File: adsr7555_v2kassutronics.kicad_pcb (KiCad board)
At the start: 2 copper layers, 78.7 x 106.7 mm, 43 parts, among them J1 Power, J2 GateIn, J5 InvOut, J6 Output, Q1 3904, Q2 3904, Q3 3904, SW1 SW_Trig, U1 7555, U2 TL074

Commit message: wiring TL074 needs checking
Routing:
- net GND: track 336.9 -> 340.5 mm, vias 2 -> 4
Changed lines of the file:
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@@
 		(tags "Resistor Axial_DIN0204 series Axial Horizontal pin pitch 7.62mm 0.167W length 3.6mm diameter 1.6mm")
 		(property "Reference" "R16"
-			(at 10.5 0.24 90)
+			(at 0 2.54 180)
 			(layer "F.SilkS")
 			(effects
@@
 		)
 		(property "Value" "1k"
-			(at 9.2 0.44 90)
+			(at 5.08 2.54 180)
 			(layer "F.Fab")
 			(effects
@@
 	)
 	(segment
+		(start 106.68 86.36)
+		(end 104.14 88.9)
+		(width 0.5)
+		(layer "F.Cu")
+		(net "GND")
+	)
+	(segment
 		(start 109.22 83.82)
 		(end 114.3 83.82)
@@
 		(net "GND")
 	)
+	(segment
+		(start 104.14 88.9)
+		(end 86.36 88.9)
+		(width 0.5)
+		(layer "F.Cu")
+		(net "GND")
+	)
+	(via
+		(at 86.36 88.9)
+		(size 0.6)
+		(drill 0.3)
+		(layers "F.Cu" "B.Cu")
+		(net "GND")
+	)
 	(via
 		(at 109.22 83.82)
@@
 	)
 	(via
-		(at 114.3 127)
+		(at 106.68 86.36)
 		(size 0.6)
 		(drill 0.3)
@@
 		(net "GND")
 	)
-	(segment
-		(start 109.22 83.82)
-		(end 101.6 83.82)
-		(width 0.5)
-		(layer "B.Cu")
+	(via
+		(at 114.3 127)
+		(size 0.6)
+		(drill 0.3)
+		(layers "F.Cu" "B.Cu")
 		(net "GND")
 	)
@@
 	)
 	(segment
+		(start 109.22 83.82)
+		(end 106.68 86.36)
+		(width 0.5)
+		(layer "B.Cu")
+		(net "GND")
+	)
+	(segment
 		(start 109.22 30.48)
 		(end 109.22 33.02)
@@
 	)
 	(segment
+		(start 86.36 83.82)
+		(end 86.36 88.9)
+		(width 0.5)
+		(layer "B.Cu")
+		(net "GND")
+	)
+	(segment
 		(start 96.52 114.3)
 		(end 93.98 116.84)
@@
 	)
 	(segment
-		(start 86.36 81.28)
-		(end 86.36 83.82)
-		(width 0.5)
-		(layer "B.Cu")
-		(net "GND")
-	)
-	(segment
 		(start 48.3 101.6)
 		(end 45.72 101.6)
@@
 	)
 	(segment
-		(start 101.6 83.82)
-		(end 99.06 81.28)
-		(width 0.5)
-		(layer "B.Cu")
-		(net "GND")
-	)
-	(segment
 		(start 48.26 66.04)
 		(end 45.72 66.04)
@@
 	)
 	(segment
-		(start 99.06 81.28)
-		(end 86.36 81.28)
-		(width 0.5)
-		(layer "B.Cu")
-		(net "GND")
-	)
-	(segment
 		(start 45.72 43.18)
 		(end 60.96 30.48)
@@
 	(segment
 		(start 76.2 88.9)
-		(end 76.2 109.22)
+		(end 76.2 101.6)
 		(width 0.5)
 		(layer "F.Cu")
@@
 	)
 	(via
-		(at 76.2 109.22)
+		(at 76.2 101.6)
 		(size 0.6)
 		(drill 0.3)
@@
 	)
 	(segment
-		(start 91.44 78.74)
-		(end 76.2 78.74)
+		(start 76.2 101.6)
+		(end 76.2 109.22)
 		(width 0.5)
 		(layer "B.Cu")
@@
 	)
 	(segment
-		(start 88.9 111.76)
-		(end 88.9 124.46)
+		(start 91.44 78.74)
+		(end 76.2 78.74)
 		(width 0.5)
 		(layer "B.Cu")
@@
 	)
 	(segment
-		(start 76.2 109.22)
-		(end 81.28 109.22)
+		(start 88.9 111.76)
+		(end 88.9 124.46)
 		(width 0.5)
 		(layer "B.Cu")
@@
 	)
 	(segment
-		(start 81.28 109.22)
-		(end 83.82 111.76)
+		(start 91.44 76.2)
+		(end 91.44 78.74)
 		(width 0.5)
 		(layer "B.Cu")
@@
 	)
 	(segment
-		(start 91.44 76.2)
-		(end 91.44 78.74)
+		(start 76.2 109.22)
+		(end 81.28 109.22)
+		(width 0.5)
+		(layer "B.Cu")
+		(net "THR")
+	)
+	(segment
+		(start 83.82 111.76)
+		(end 81.28 109.22)
 		(width 0.5)
 		(layer "B.Cu")

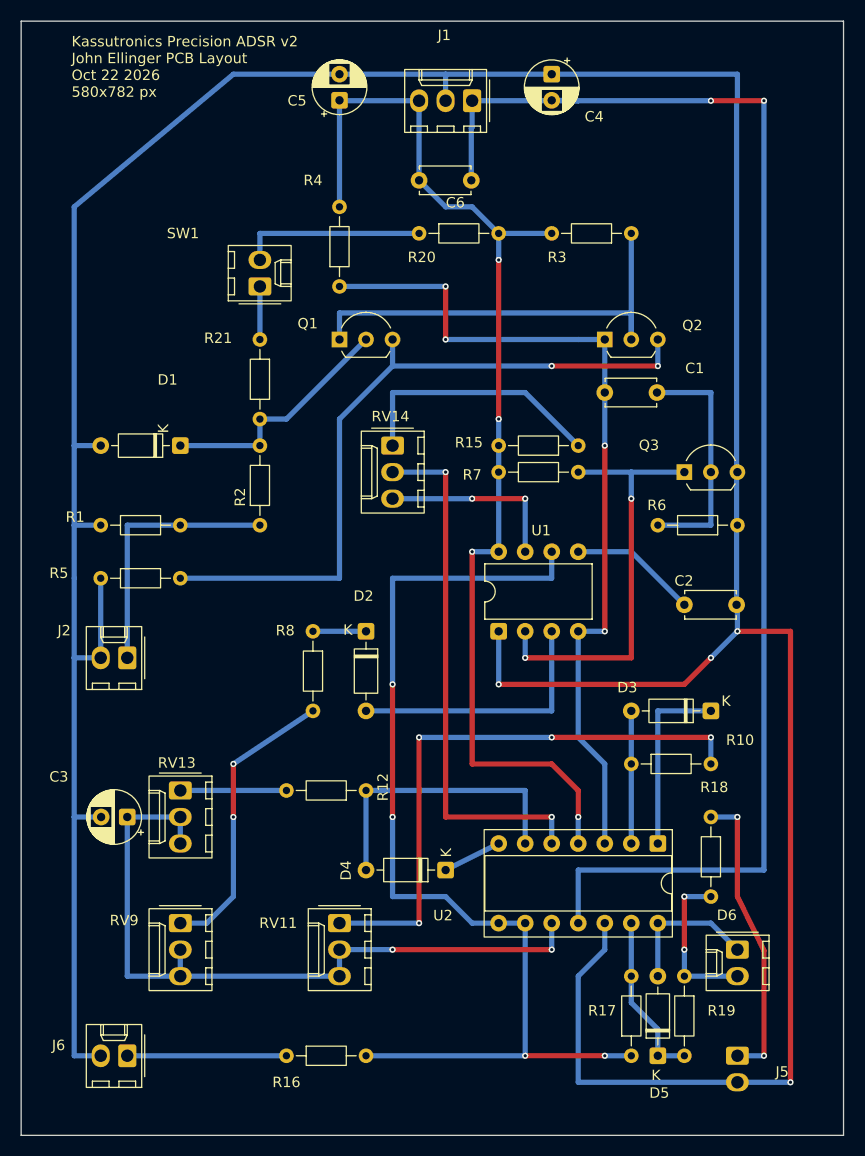
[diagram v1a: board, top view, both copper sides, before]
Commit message: MAJOR FUP U2 was positioned backwards. Involved pt to pt silicon wires on bottom of PCB. Still not done
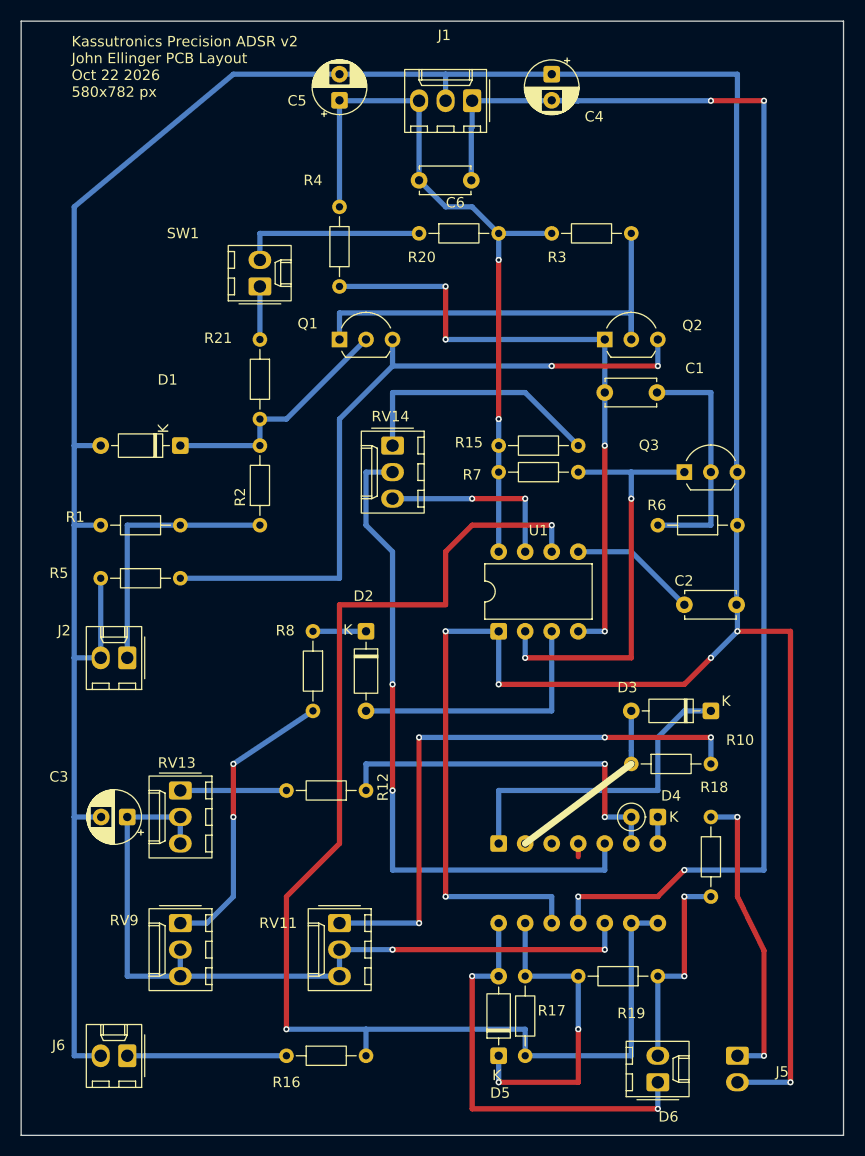
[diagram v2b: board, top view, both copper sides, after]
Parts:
- D4: footprint Diode_THT:D_DO-35_SOD27_P7.62mm_Horizontal -> Diode_THT:D_DO-35_SOD27_P2.54mm_Vertical_CathodeUp
- U2: moved to B.Cu
- moved D4 20.9 mm to (101.6, 101.6)
- moved D5 15.2 mm to (86.4, 124.5)
- moved U2 15.2 mm to (86.4, 104.1)
- moved D6 14.8 mm to (101.6, 127.0), turned to 90 degrees
- moved R17 10.2 mm to (88.9, 124.5)
- moved R19 2.54 mm to (101.6, 116.8), turned to 180 degrees
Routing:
- net +15V: track 109.9 -> 72.0 mm, vias 4 -> 2
- net Net-(D5-A): track 13.8 -> 40.6 mm, vias 0 -> 2
- net THR: track 100.1 -> 125.1 mm, vias 4 -> 2
- net GATE: track 82.3 -> 61.0 mm
- net Net-(D5-K): track 16.3 -> 30.5 mm, vias 0 -> 2
- net Net-(U2B-+): track 50.8 -> 64.6 mm
- net Net-(D3-K): track 17.8 -> 31.5 mm
- net GND: track 340.5 -> 352.1 mm, vias 4 -> 6
- net Net-(D4-A): track 27.9 -> 35.6 mm, vias 0 -> 2
- net Net-(D3-A): track 12.7 -> 5.08 mm
- net Net-(D6-A): track 15.2 -> 20.3 mm
- net Net-(U2C-+): track 71.1 -> 76.2 mm
- net Net-(D4-K): track 5.68 -> 2.54 mm
- net -15V: track 134.7 -> 133.2 mm, vias 2 -> 4
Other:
- board text added: "1"

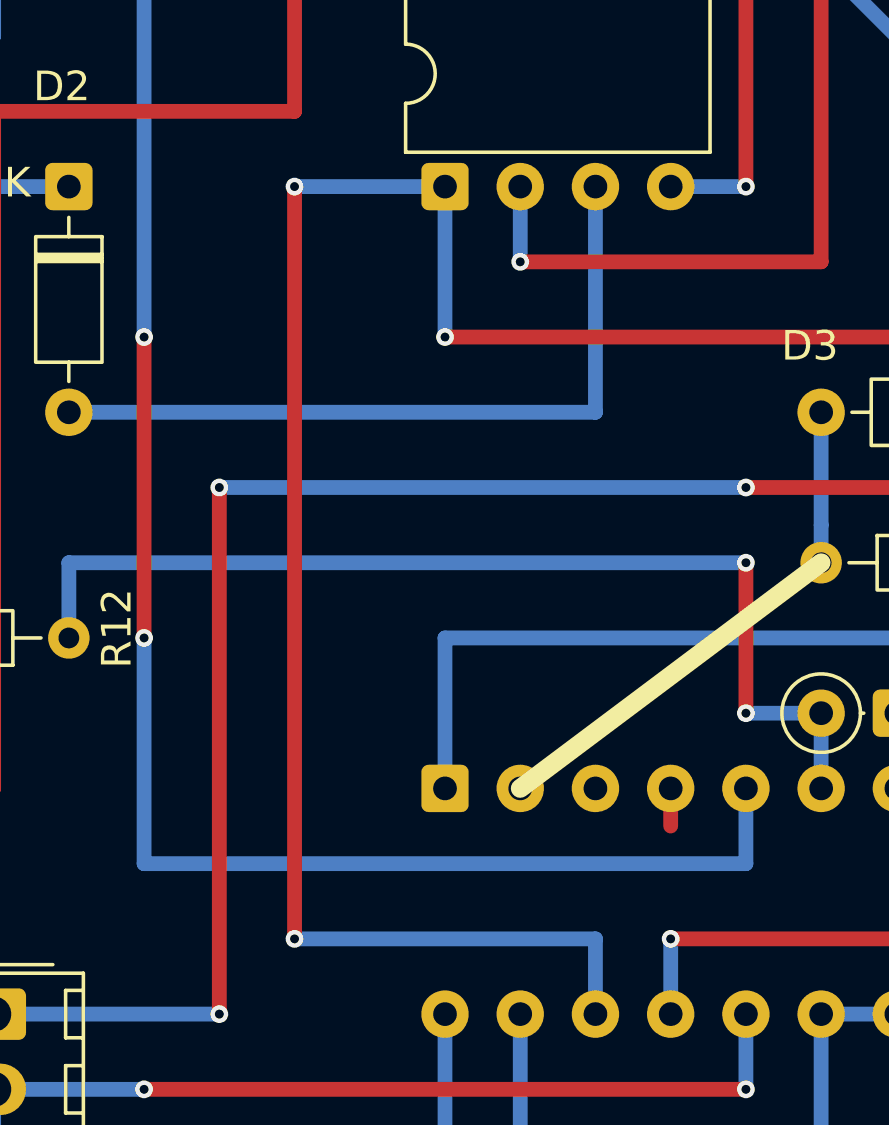
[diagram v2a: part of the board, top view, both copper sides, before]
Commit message: wired +15 -15 gnd
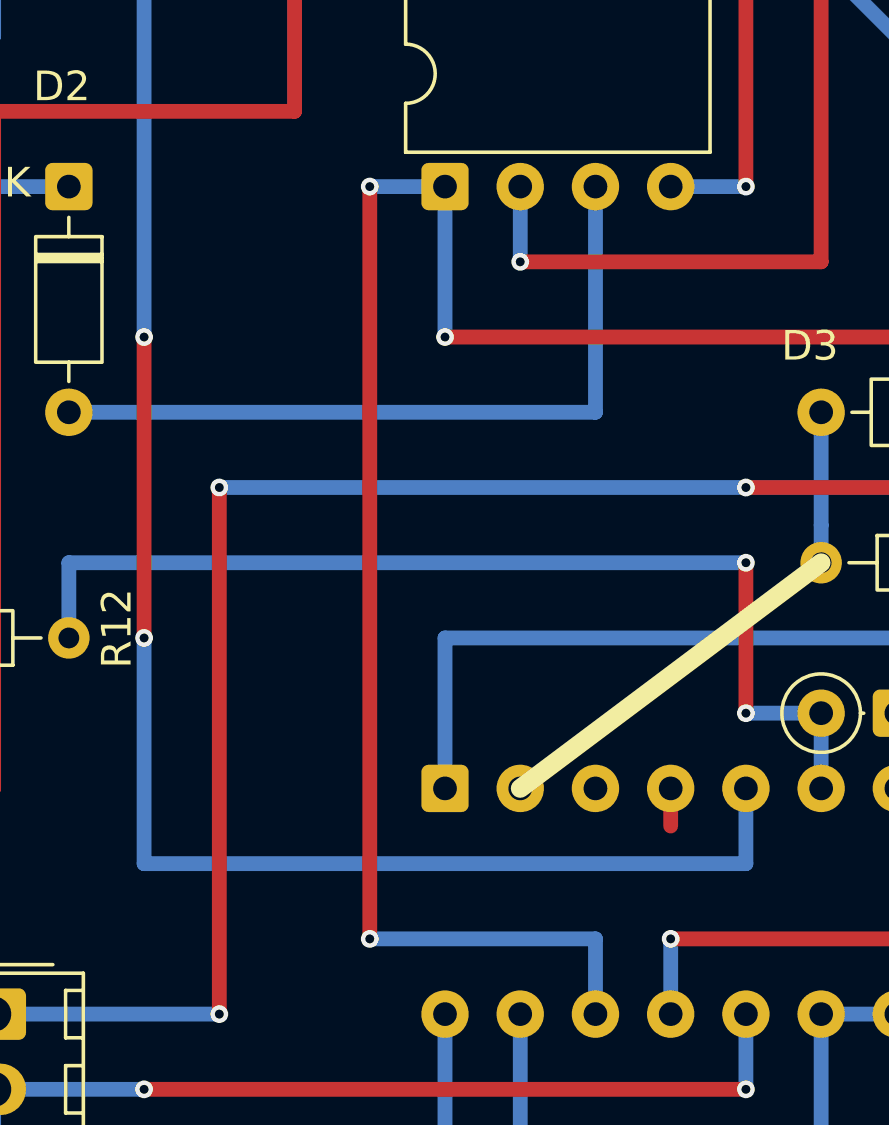
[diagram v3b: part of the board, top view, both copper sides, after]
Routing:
- net GND: track 352.1 -> 347.1 mm

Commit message: wiring L074 area in progress
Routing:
- net THR: track 125.1 -> 111.8 mm, vias 2 -> 4
- net Net-(D3-K): track 31.5 -> 40.6 mm
- net Net-(U2B-+): track 64.6 -> 61.0 mm, vias 2 -> 4
- net Net-(J5-Pin_1): track 28.5 -> 27.9 mm
- net -15V: vias 4 -> 2
- net Net-(D6-A): vias 2 -> 0
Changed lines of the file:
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@@
 			(at -1.62 0.32 90)
 			(layer "F.SilkS")
+			(hide yes)
 			(effects
 				(font
@@
 	)
 	(segment
-		(start 71.12 104.14)
-		(end 71.12 81.28)
-		(width 0.5)
-		(layer "F.Cu")
-		(net "THR")
-	)
-	(segment
-		(start 66.04 121.92)
-		(end 66.04 109.22)
+		(start 76.2 73.66)
+		(end 76.2 119.38)
 		(width 0.5)
 		(layer "F.Cu")
@@
 	)
 	(segment
-		(start 81.28 76.2)
-		(end 83.82 73.66)
-		(width 0.5)
-		(layer "F.Cu")
-		(net "THR")
-	)
-	(segment
-		(start 66.04 109.22)
-		(end 71.12 104.14)
-		(width 0.5)
-		(layer "F.Cu")
-		(net "THR")
-	)
-	(segment
-		(start 71.12 81.28)
-		(end 81.28 81.28)
+		(start 83.82 73.66)
+		(end 91.44 73.66)
 		(width 0.5)
 		(layer "F.Cu")
 		(net "THR")
 	)
-	(segment
-		(start 81.28 81.28)
-		(end 81.28 76.2)
-		(width 0.5)
-		(layer "F.Cu")
+	(via
+		(at 83.82 73.66)
+		(size 0.6)
+		(drill 0.3)
+		(layers "F.Cu" "B.Cu")
 		(net "THR")
 	)
-	(segment
-		(start 83.82 73.66)
-		(end 91.44 73.66)
-		(width 0.5)
-		(layer "F.Cu")
+	(via
+		(at 76.2 119.38)
+		(size 0.6)
+		(drill 0.3)
+		(layers "F.Cu" "B.Cu")
 		(net "THR")
 	)
 	(via
-		(at 66.04 121.92)
+		(at 76.2 73.66)
 		(size 0.6)
 		(drill 0.3)
@@
 	)
 	(segment
-		(start 73.66 121.92)
-		(end 88.9 121.92)
+		(start 76.2 121.92)
+		(end 78.74 121.92)
 		(width 0.5)
 		(layer "B.Cu")
@@
 	)
 	(segment
-		(start 73.66 121.92)
-		(end 66.04 121.92)
+		(start 91.44 76.2)
+		(end 91.44 73.66)
 		(width 0.5)
 		(layer "B.Cu")
@@
 	)
 	(segment
-		(start 91.44 76.2)
-		(end 91.44 73.66)
+		(start 78.74 121.92)
+		(end 88.9 121.92)
 		(width 0.5)
 		(layer "B.Cu")
@@
 	)
 	(segment
+		(start 76.2 121.92)
+		(end 76.2 119.38)
+		(width 0.5)
+		(layer "B.Cu")
+		(net "THR")
+	)
+	(segment
+		(start 83.82 73.66)
+		(end 76.2 73.66)
+		(width 0.5)
+		(layer "B.Cu")
+		(net "THR")
+	)
+	(segment
 		(start 73.66 124.46)
 		(end 73.66 121.92)
@@
 	)
 	(segment
+		(start 73.66 121.92)
+		(end 76.2 121.92)
+		(width 0.5)
+		(layer "B.Cu")
+		(net "THR")
+	)
+	(segment
 		(start 99.06 124.46)
 		(end 99.06 111.76)
@@
 	)
 	(segment
-		(start 76.2 114.3)
+		(start 78.74 114.3)
 		(end 96.52 114.3)
 		(width 0.5)
@@
 	)
 	(via
-		(at 76.2 114.3)
+		(at 78.74 114.3)
 		(size 0.6)
 		(drill 0.3)
@@
 	(segment
 		(start 71.12 114.3)
-		(end 76.2 114.3)
+		(end 78.74 114.3)
 		(width 0.5)
 		(layer "B.Cu")
@@
 		(net "Net-(J5-Pin_1)")
 	)
-	(segment
-		(start 111.76 114.378122)
-		(end 111.76 124.46)
-		(width 0.5)
-		(layer "F.Cu")
-		(net "Net-(J5-Pin_1)")
-	)
-	(segment
-		(start 109.22 109.22)
-		(end 111.76 114.378122)
-		(width 0.5)
-		(layer "F.Cu")
-		(net "Net-(J5-Pin_1)")
-	)
 	(via
 		(at 109.22 101.6)
@@
 	)
 	(via
-		(at 111.76 124.46)
+		(at 109.22 109.22)
 		(size 0.6)
 		(drill 0.3)
@@
 	)
 	(segment
+		(start 109.22 124.46)
+		(end 109.22 109.22)
+		(width 0.5)
+		(layer "B.Cu")
+		(net "Net-(J5-Pin_1)")
+	)
+	(segment
 		(start 111.76 124.46)
 		(end 109.22 124.46)
@@
 	)
 	(segment
-		(start 104.14 116.84)
-		(end 104.14 109.22)
+		(start 101.6 124.46)
+		(end 101.6 116.84)
 		(width 0.5)
-		(layer "F.Cu")
-		(net "Net-(D6-A)")
-	)
-	(via
-		(at 104.14 116.84)
-		(size 0.6)
-		(drill 0.3)
-		(layers "F.Cu" "B.Cu")
-		(net "Net-(D6-A)")
-	)
-	(via
-		(at 104.14 109.22)
-		(size 0.6)
-		(drill 0.3)
-		(layers "F.Cu" "B.Cu")
+		(layer "B.Cu")
 		(net "Net-(D6-A)")
 	)
 	(segment
-		(start 101.6 124.46)
-		(end 101.6 116.84)
+		(start 104.14 109.22)
+		(end 106.68 109.22)
 		(width 0.5)
 		(layer "B.Cu")
@@
 	(segment
 		(start 104.14 109.22)
-		(end 106.68 109.22)
+		(end 104.14 116.84)
 		(width 0.5)
 		(layer "B.Cu")
@@
 	)
 	(segment
-		(start 76.2 99.06)
-		(end 76.2 88.9)
+		(start 81.28 88.9)
+		(end 81.28 106.68)
+		(width 0.5)
+		(layer "F.Cu")
+		(net "Net-(U2B-+)")
+	)
+	(segment
+		(start 81.28 68.58)
+		(end 81.28 86.36)
 		(width 0.5)
 		(layer "F.Cu")
@@
 	)
 	(via
-		(at 76.2 99.06)
+		(at 81.28 68.58)
 		(size 0.6)
 		(drill 0.3)
@@
 	)
 	(via
-		(at 76.2 88.9)
+		(at 81.28 106.68)
 		(size 0.6)
 		(drill 0.3)
@@
 		(net "Net-(U2B-+)")
 	)
-	(segment
-		(start 96.52 104.14)
-		(end 96.52 106.68)
-		(width 0.5)
-		(layer "B.Cu")
-		(net "Net-(U2B-+)")
-	)
-	(segment
-		(start 96.52 106.68)
-		(end 76.2 106.68)
-		(width 0.5)
-		(layer "B.Cu")
+	(via
+		(at 81.28 86.36)
+		(size 0.6)
+		(drill 0.3)
+		(layers "F.Cu" "B.Cu")
 		(net "Net-(U2B-+)")
 	)
-	(segment
-		(start 76.2 88.9)
-		(end 76.2 76.2)
-		(width 0.5)
-		(layer "B.Cu")
+	(via
+		(at 81.28 88.9)
+		(size 0.6)
+		(drill 0.3)
+		(layers "F.Cu" "B.Cu")
 		(net "Net-(U2B-+)")
 	)
 	(segment
-		(start 76.2 76.2)
-		(end 73.66 73.66)
+		(start 76.2 68.58)
+		(end 81.28 68.58)
 		(width 0.5)
 		(layer "B.Cu")
@@
 	)
 	(segment
-		(start 73.66 68.58)
-		(end 76.2 68.58)
+		(start 96.52 106.68)
+		(end 96.52 104.14)
 		(width 0.5)
 		(layer "B.Cu")
@@
 	)
 	(segment
-		(start 73.66 73.66)
-		(end 73.66 68.58)
+		(start 81.28 86.36)
+		(end 81.28 88.9)
 		(width 0.5)
 		(layer "B.Cu")
@@
 	)
 	(segment
-		(start 76.2 106.68)
-		(end 76.2 99.06)
+		(start 81.28 106.68)
+		(end 96.52 106.68)
 		(width 0.5)
 		(layer "B.Cu")
@@
 	)
 	(segment
-		(start 101.6 93.98)
-		(end 104.14 91.44)
-		(width 0.5)
-		(layer "B.Cu")
-		(net "Net-(D3-K)")
-	)
-	(segment
 		(start 86.36 104.14)
 		(end 86.36 99.06)
@@
 	)
 	(segment
-		(start 101.6 99.06)
-		(end 101.6 93.98)
+		(start 104.14 91.44)
+		(end 106.68 91.44)
 		(width 0.5)
 		(layer "B.Cu")
@@
 	)
 	(segment
-		(start 104.14 91.44)
+		(start 109.22 91.44)
 		(end 106.68 91.44)
 		(width 0.5)
@@
 	)
 	(segment
-		(start 86.36 99.06)
-		(end 101.6 99.06)
+		(start 109.22 99.06)
+		(end 109.22 91.44)
 		(width 0.5)
 		(layer "B.Cu")
@@
 	)
 	(segment
-		(start 104.14 106.68)
-		(end 101.6 109.22)
-		(width 0.5)
-		(layer "F.Cu")
-		(net "-15V")
-	)
-	(segment
-		(start 101.6 109.22)
-		(end 93.98 109.22)
+		(start 86.36 99.06)
+		(end 109.22 99.06)
 		(width 0.5)
-		(layer "F.Cu")
-		(net "-15V")
+		(layer "B.Cu")
+		(net "Net-(D3-K)")
 	)
 	(segment
@@
 		(net "-15V")
 	)
-	(via
-		(at 93.98 109.22)
-		(size 0.6)
-		(drill 0.3)
-		(layers "F.Cu" "B.Cu")
-		(net "-15V")
-	)
-	(via
-		(at 104.14 106.68)
-		(size 0.6)
-		(drill 0.3)
-		(layers "F.Cu" "B.Cu")
-		(net "-15V")
-	)
 	(segment
-		(start 93.98 109.22)
-		(end 93.98 111.76)
+		(start 111.76 106.68)
+		(end 111.76 33.02)
 		(width 0.5)
 		(layer "B.Cu")
@@
 	)
 	(segment
-		(start 91.44 32.98)
-		(end 93.98 33.02)
+		(start 93.98 109.22)
+		(end 99.06 109.22)
 		(width 0.5)
 		(layer "B.Cu")
@@
 	)
 	(segment
-		(start 111.76 106.68)
-		(end 104.14 106.68)
+		(start 91.44 32.98)
+		(end 93.98 33.02)
 		(width 0.5)
 		(layer "B.Cu")
@@
 	)
 	(segment
-		(start 93.98 33.02)
-		(end 106.68 33.02)
+		(start 93.98 111.76)
+		(end 93.98 109.22)
 		(width 0.5)
 		(layer "B.Cu")
@@
 	)
 	(segment
-		(start 111.76 33.02)
-		(end 111.76 106.68)
+		(start 93.98 33.02)
+		(end 106.68 33.02)
 		(width 0.5)
 		(layer "B.Cu")
@@
 		(width 0.5)
 		(layer "B.Cu")
+		(net "-15V")
+	)
+	(segment
+		(start 101.6 106.68)
+		(end 111.76 106.68)
+		(width 0.5)
+		(layer "B.Cu")
+		(net "-15V")
+	)
+	(segment
+		(start 99.06 109.22)
+		(end 101.6 106.68)
+		(width 0.5)
+		(layer "B.Cu")
